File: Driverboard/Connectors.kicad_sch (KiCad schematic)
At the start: 14 parts

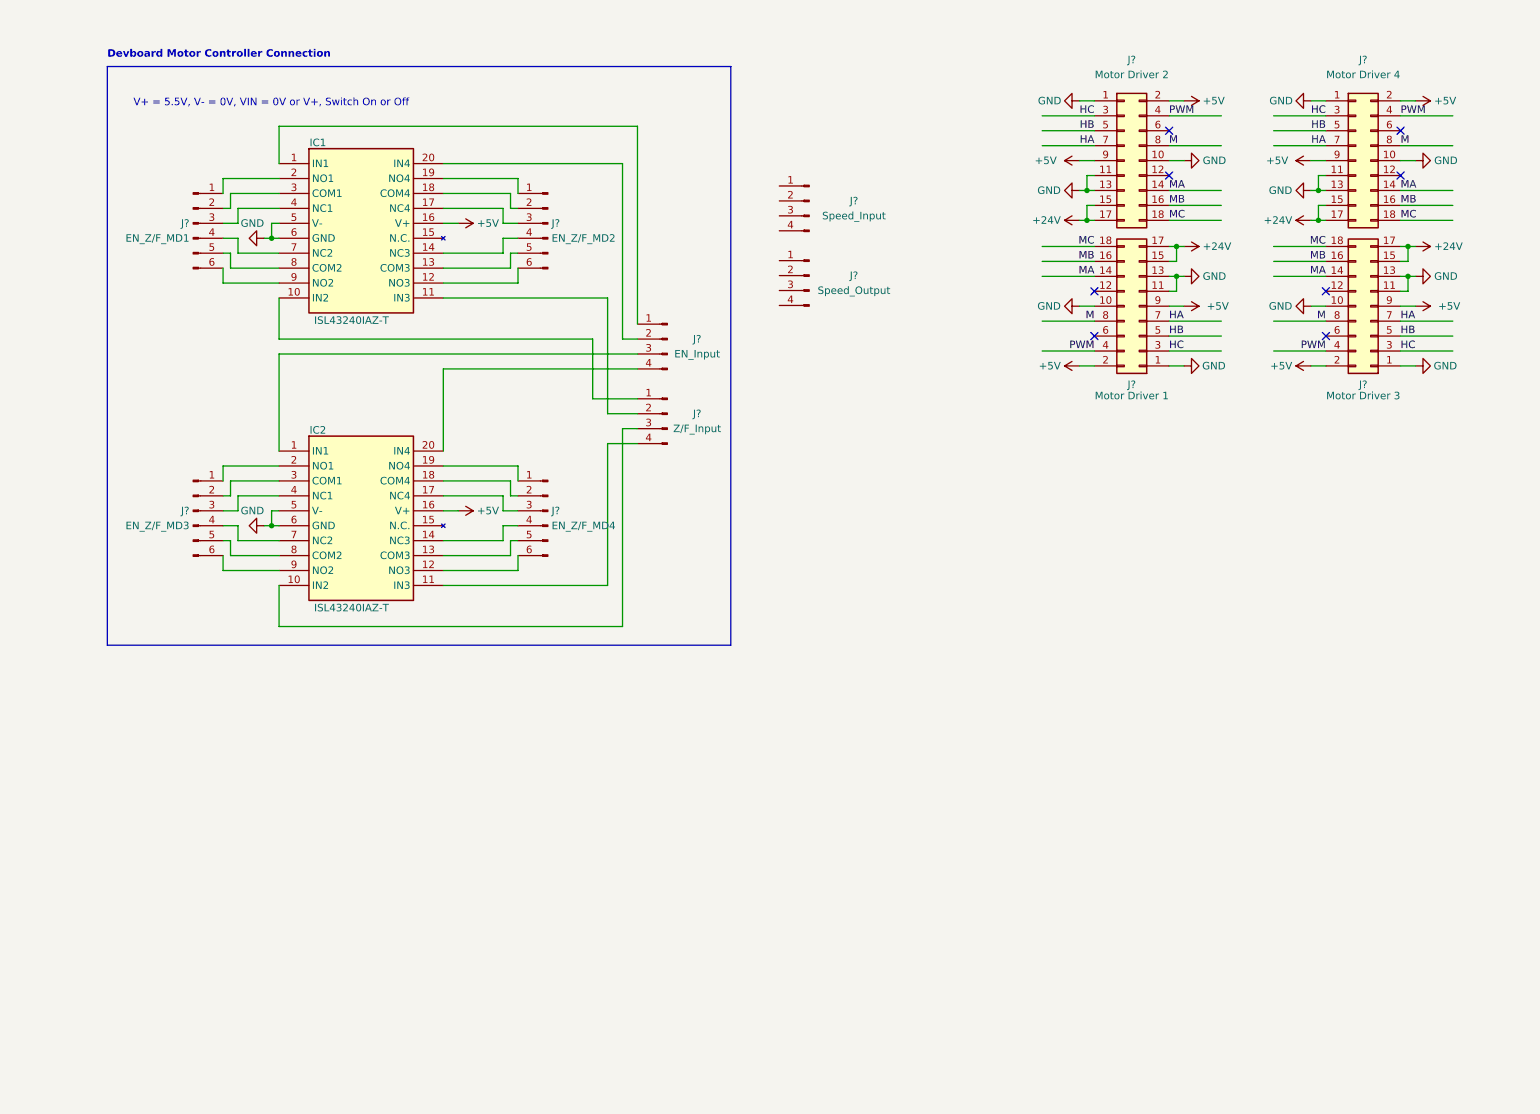
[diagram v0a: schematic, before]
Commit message: Motor Driver complete
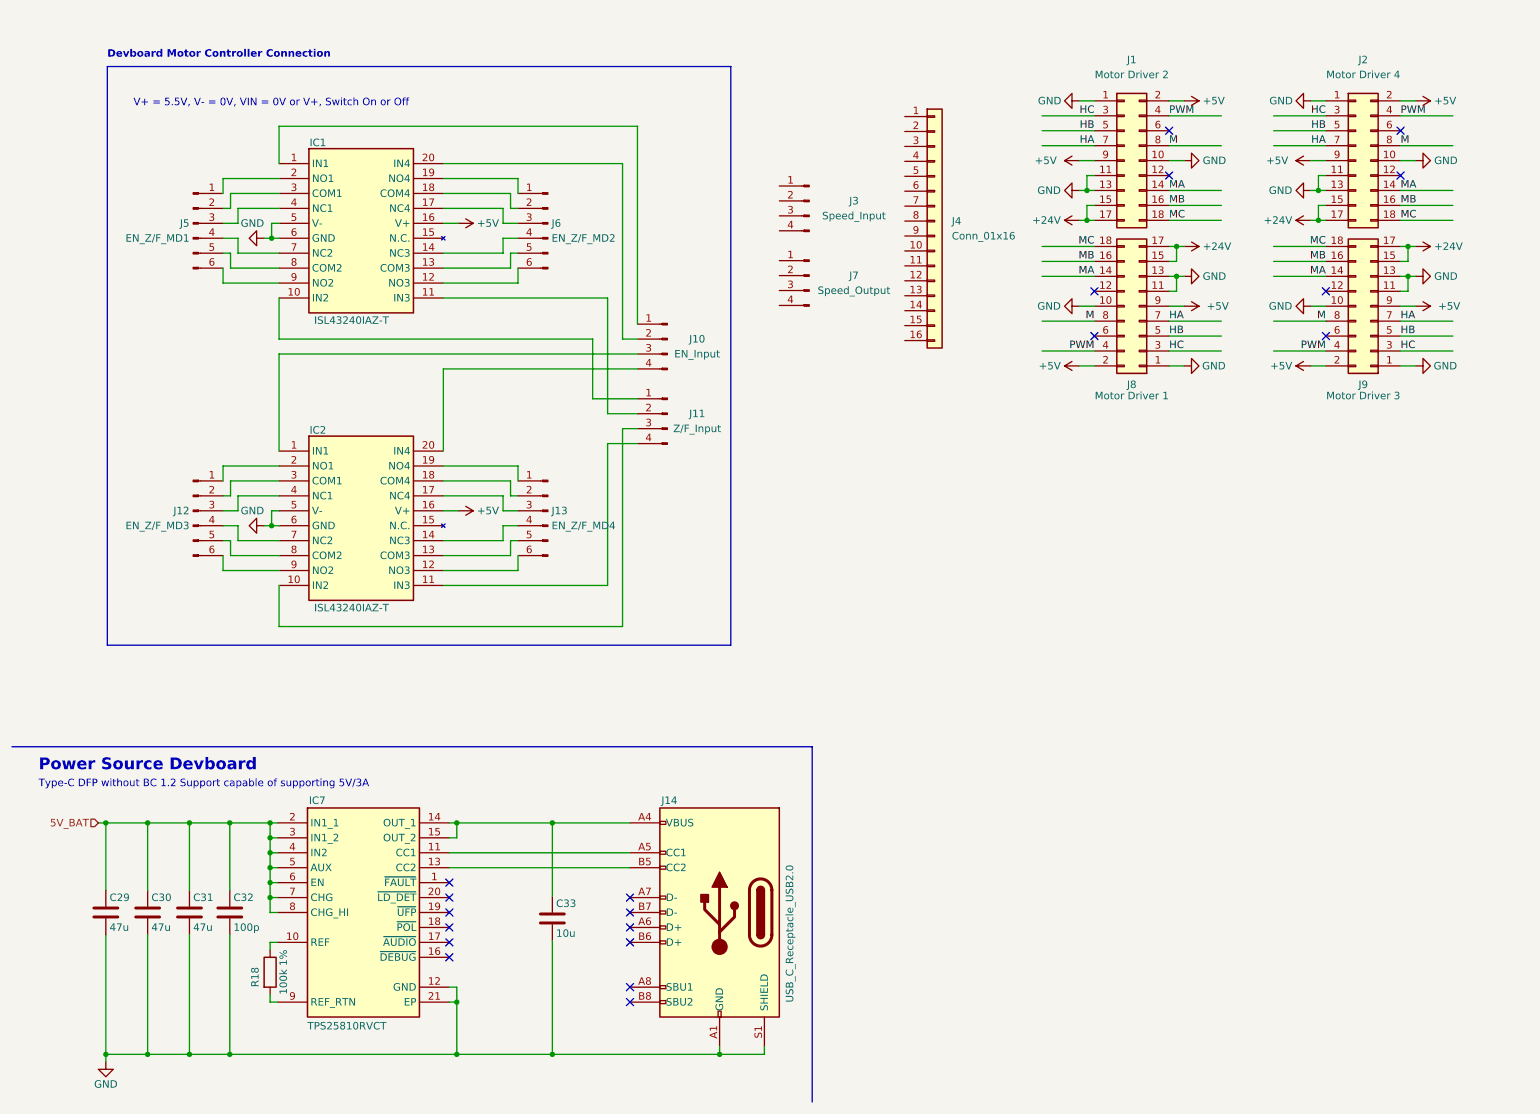
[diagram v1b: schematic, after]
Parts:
- added C29, C30, C31: 47u, symbol Device:C
- added C32: 100p, symbol Device:C
- added C33: 10u, symbol Device:C
- added IC7: TPS25810RVCT, symbol TPS25810RVCT:TPS25810RVCT
- added J14: USB_C_Receptacle_USB2.0, symbol Connector:USB_C_Receptacle_USB2.0
- added J4: Conn_01x16, symbol Connector_Generic:Conn_01x16
- added R18: 100k 1%, symbol Device:R
- gave numbers to parts that had none: 14
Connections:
- net GND: now also C29.2, C30.2, C31.2, C32.2, C33.2, IC7.12 (GND), IC7.21 (EP), J14.A1 (GND), J14.A12 (GND), J14.B1 (GND), J14.B12 (GND), J14.S1 (SHIELD)
- new net: IC7.10 (REF), R18.1
- new net: IC7.9 (REF_RTN), R18.2
- new net: C33.1, IC7.14 (OUT_1), IC7.15 (OUT_2), J14.A4 (VBUS), J14.A9 (VBUS), J14.B4 (VBUS), J14.B9 (VBUS)
- new net: IC7.11 (CC1), J14.A5 (CC1)
- new net: IC7.13 (CC2), J14.B5 (CC2)
- new net 5V_BAT: C29.1, C30.1, C31.1, C32.1, IC7.2 (IN1_1), IC7.3 (IN1_2), IC7.4 (IN2), IC7.5 (AUX), IC7.6 (EN), IC7.7 (CHG), IC7.8 (CHG_HI)
- no-connect marks 8 -> 20
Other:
- note added: "Power Source Devboard"
- note added: "Type-C DFP without BC 1.2 Support capable of supporting 5V/3A"

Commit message: WIP
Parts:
- added 1: TPS25854QRPQRQ1, symbol TPS25854QRPQRQ1:TPS25854QRPQRQ1
- added C34, C35, C36, C37, C38, C39, C40, C41: C, symbol Device:C
- added L7: L, symbol Device:L
- added R19, R20, R21, R23, R24, R25, R26: R, symbol Device:R
- added R22: R_Variable, symbol Device:R_Variable
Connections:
- net GND: now also 1.16 (PGND_1), 1.24 (PGND_2), 1.25 (PGND_3), C34.2, C35.2, C37.2, C38.2, C39.2, C40.2, C41.2
- new net: 1.23 (SW), C36.1, L7.1
- new net: 1.21 (BOOT_1), 1.29 (BOOT_2), C36.2
- new net: 1.2 (TS), R21.1, R22.2, R23.2
- new net: 1.20 (EN/UV), R19.1, R20.2
- new net: 1.1 (NC_1), 1.12 (NC_2), 1.26 (NC_3)
- new net: 1.14 (IMON), R24.2
- new net: 1.15 (~{THERM_WARN}), 1.17 (~{POL}), 1.18 (~{FAULT})
- new net: 1.19 (FREQ/_SYNC), R26.2
- new net: 1.27 (ILIM_2), 1.9 (ILIM_1), R25.2
- new net +BAT: 1.22 (IN), C34.1, C35.1, R19.2
- new net 5V/200mA: 1.13 (OUT_1), 1.28 (OUT_2), C41.1
- new net GNDA: 1.6 (AGND), R20.1, R23.1, R24.1, R25.1, R26.1
- new net Vsense: 1.11 (SENSE), 1.3 (BIAS), C37.1, C38.1, C39.1, C40.1, L7.2, R21.2, R22.1
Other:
- moved on the sheet: J1, J2, J3, J4, J7, J8, J9

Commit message: Powerboard v0.1, not ready for manufacturing yet
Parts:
- renumbered 1 to 11, C40 to C35, C35 to C36, C36 to C37, C37 to C38, C41 to C39, C38 to C40, C39 to C41, R24 to R19, R25 to R20, R26 to R22, R19 to R23, R20 to R24, R22 to R25, R23 to R26
